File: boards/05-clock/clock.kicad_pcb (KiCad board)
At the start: 2 copper layers, 136 x 160 mm, 54 parts, among them J1 BUS, J2 SLOW, Q1 2N7000, Q10 2N7000, Q11 2N7000, Q12 2N7000, Q13 2N7000, Q14 2N7000, Q15 2N7000, Q16 2N7000, Q2 2N7000, Q3 2N7000, Q4 2N7000, Q5 2N7000, Q6 2N7000, Q7 2N7000, Q8 2N7000, Q9 2N7000, SW1 RUN

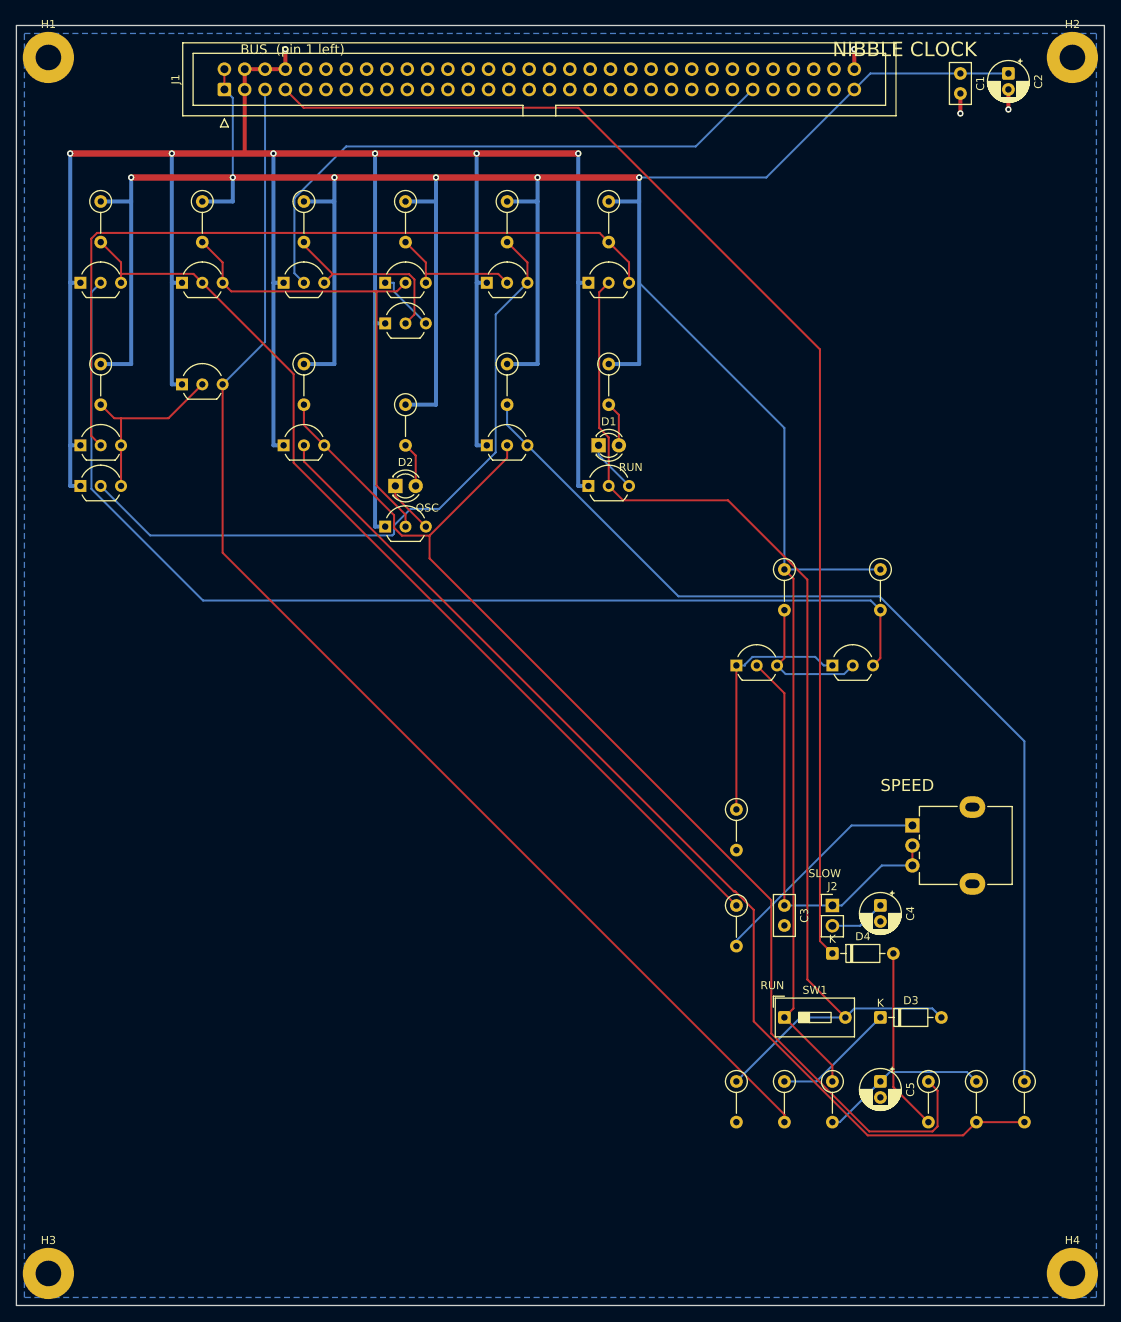
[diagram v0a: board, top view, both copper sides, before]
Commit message: Silkscreen out from under the connectors; testbench parts kept off the board
The renders showed the 'BUS (pin 1 left)' label under every top-edge
header shroud and the clock's name half under its header; the registers
board name ran into a mounting hole, and the registers testbench's four
bus-driver diodes were being loaded onto the board and parked off its
edge. Testbench symbols (refs 9000 and up) are now written with on_board
and in_bom off and pcb.py skips them too. pcb.py --silk replaces a routed
board's silk from the plan without re-routing; ALU and clock done that
way, DRC still zero. The program board's caps move beside the second
header so its label fits below it.

Co-Authored-By: Claude Fable 5.1 <noreply@anthropic.com>
Claude-Session: https://claude.ai/code/session_019vcbW37ERmrjZaWq55Er3J
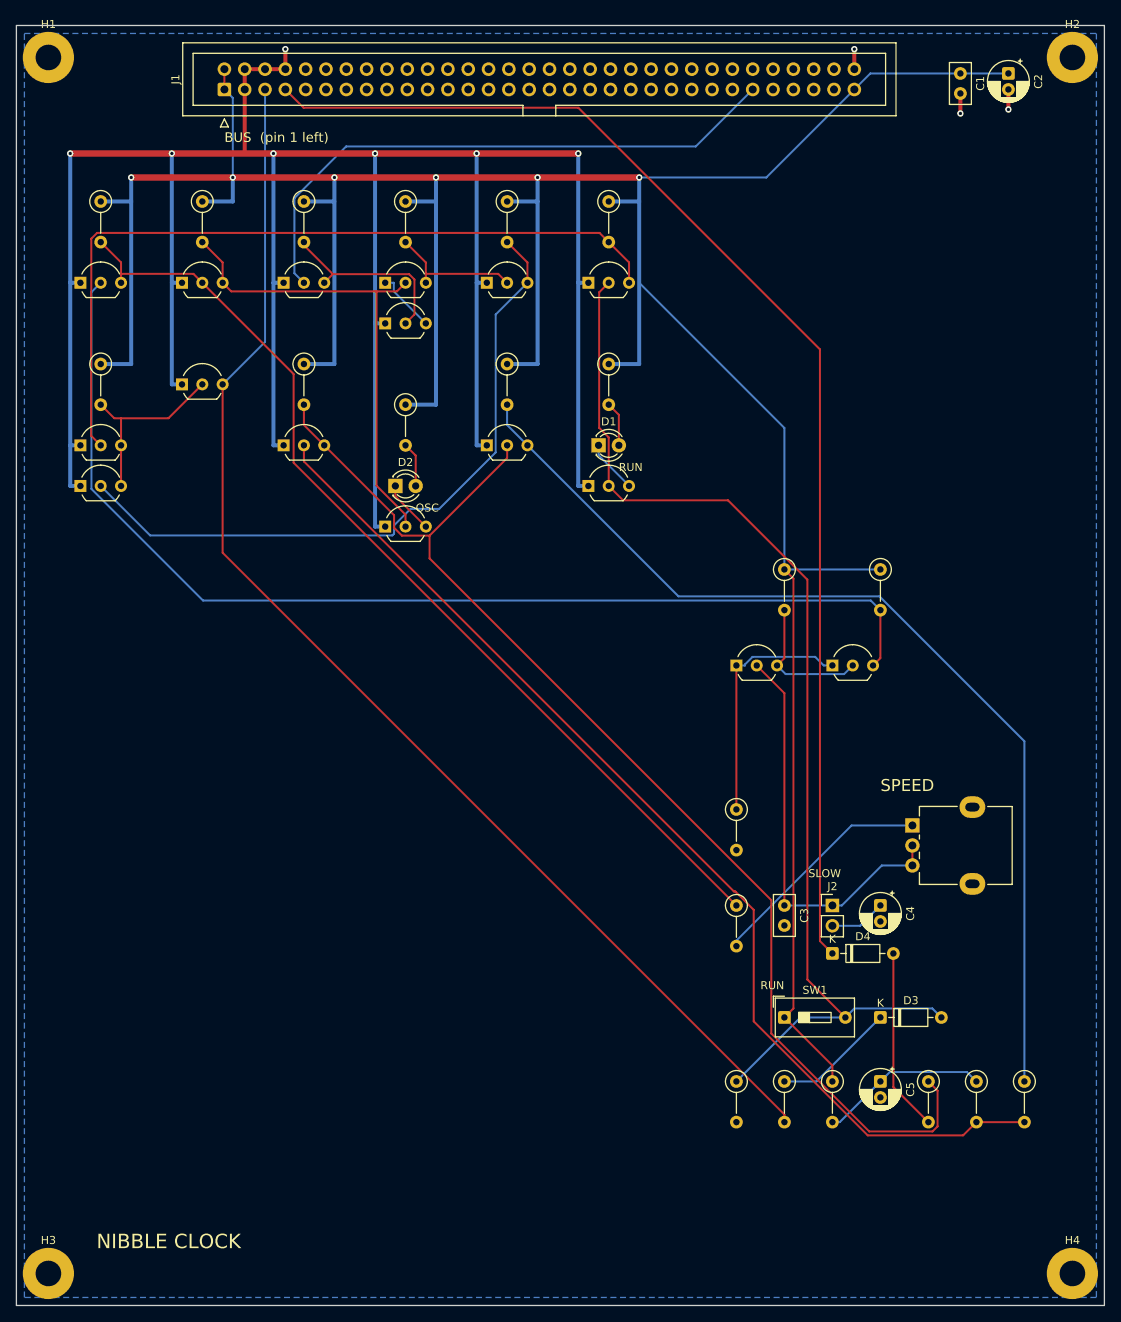
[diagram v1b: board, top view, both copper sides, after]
